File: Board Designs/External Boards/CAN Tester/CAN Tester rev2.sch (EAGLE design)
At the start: 30 parts, among them M1 Minifit-1, M2 Nanofit-1, M3 Nanofit-2, M4 Minifit-2, U1 ISOLATED CAN TRANSCIEVER, U3 TEENSY_3.2_SIMPLE, U4 CHARACTER_LCD

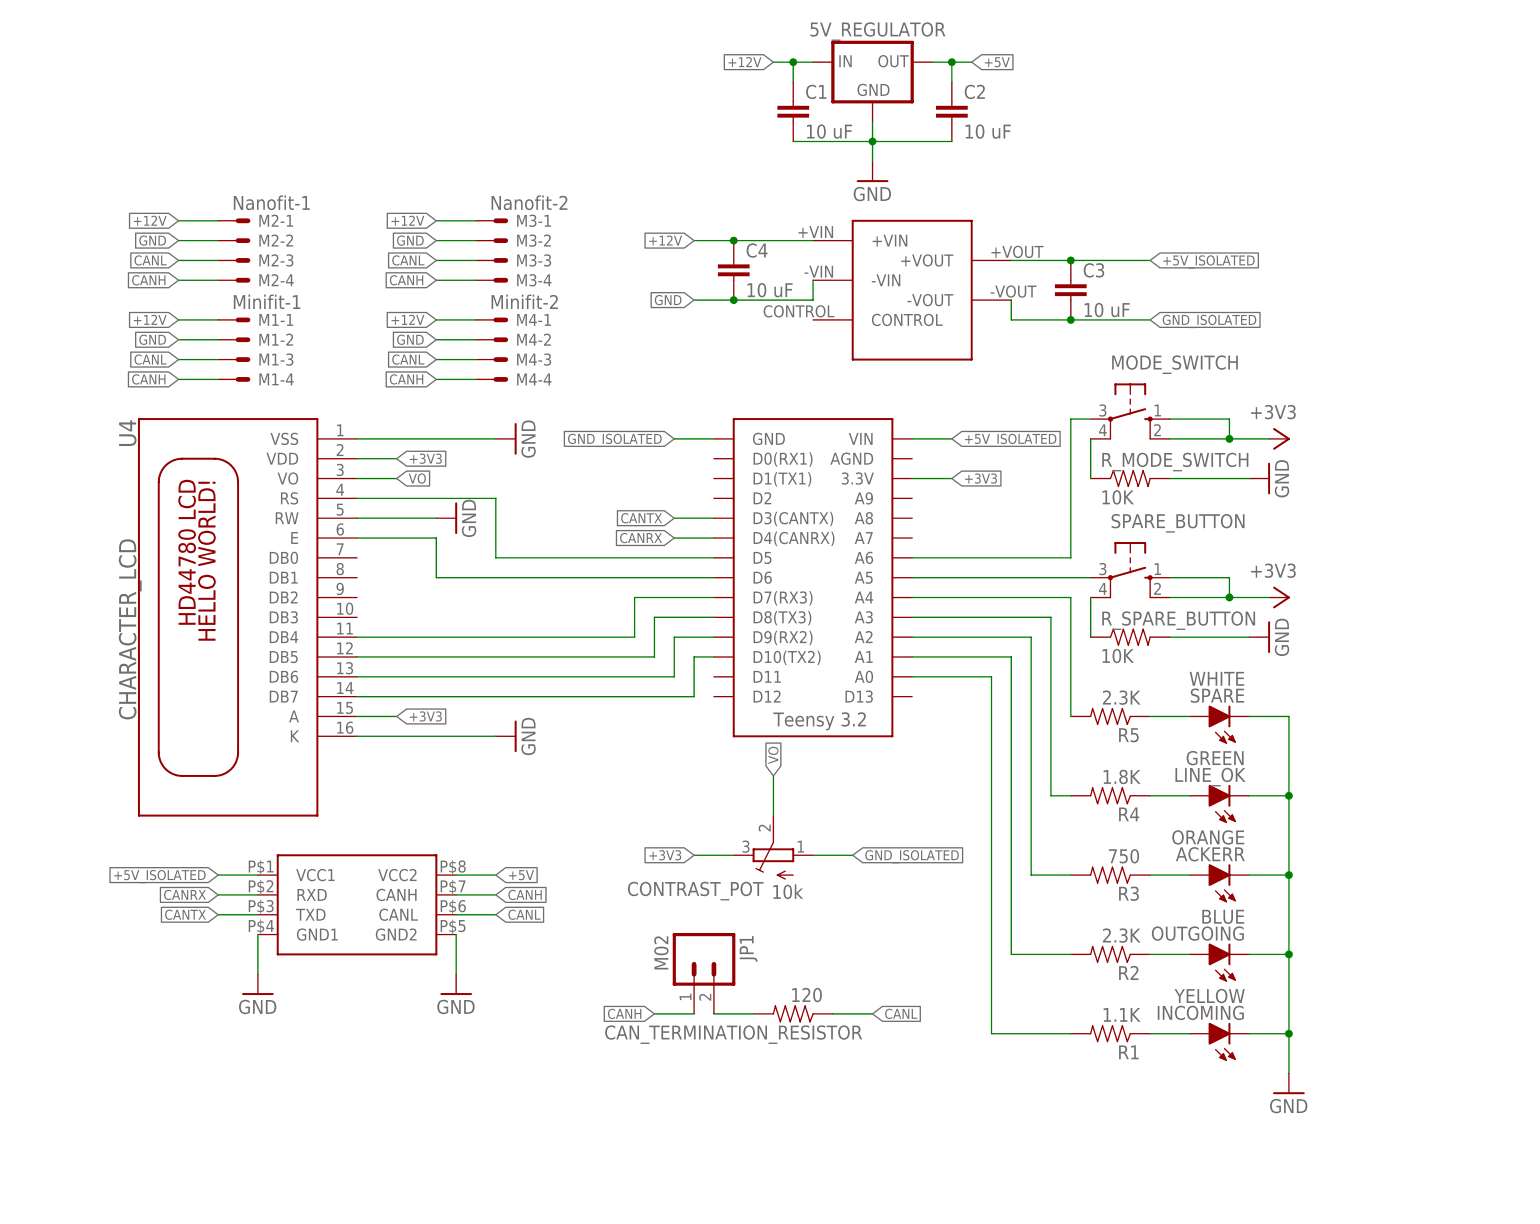
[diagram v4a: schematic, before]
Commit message: Adjusted schematic to make the connections clearer for CAN_Tester, and verified it
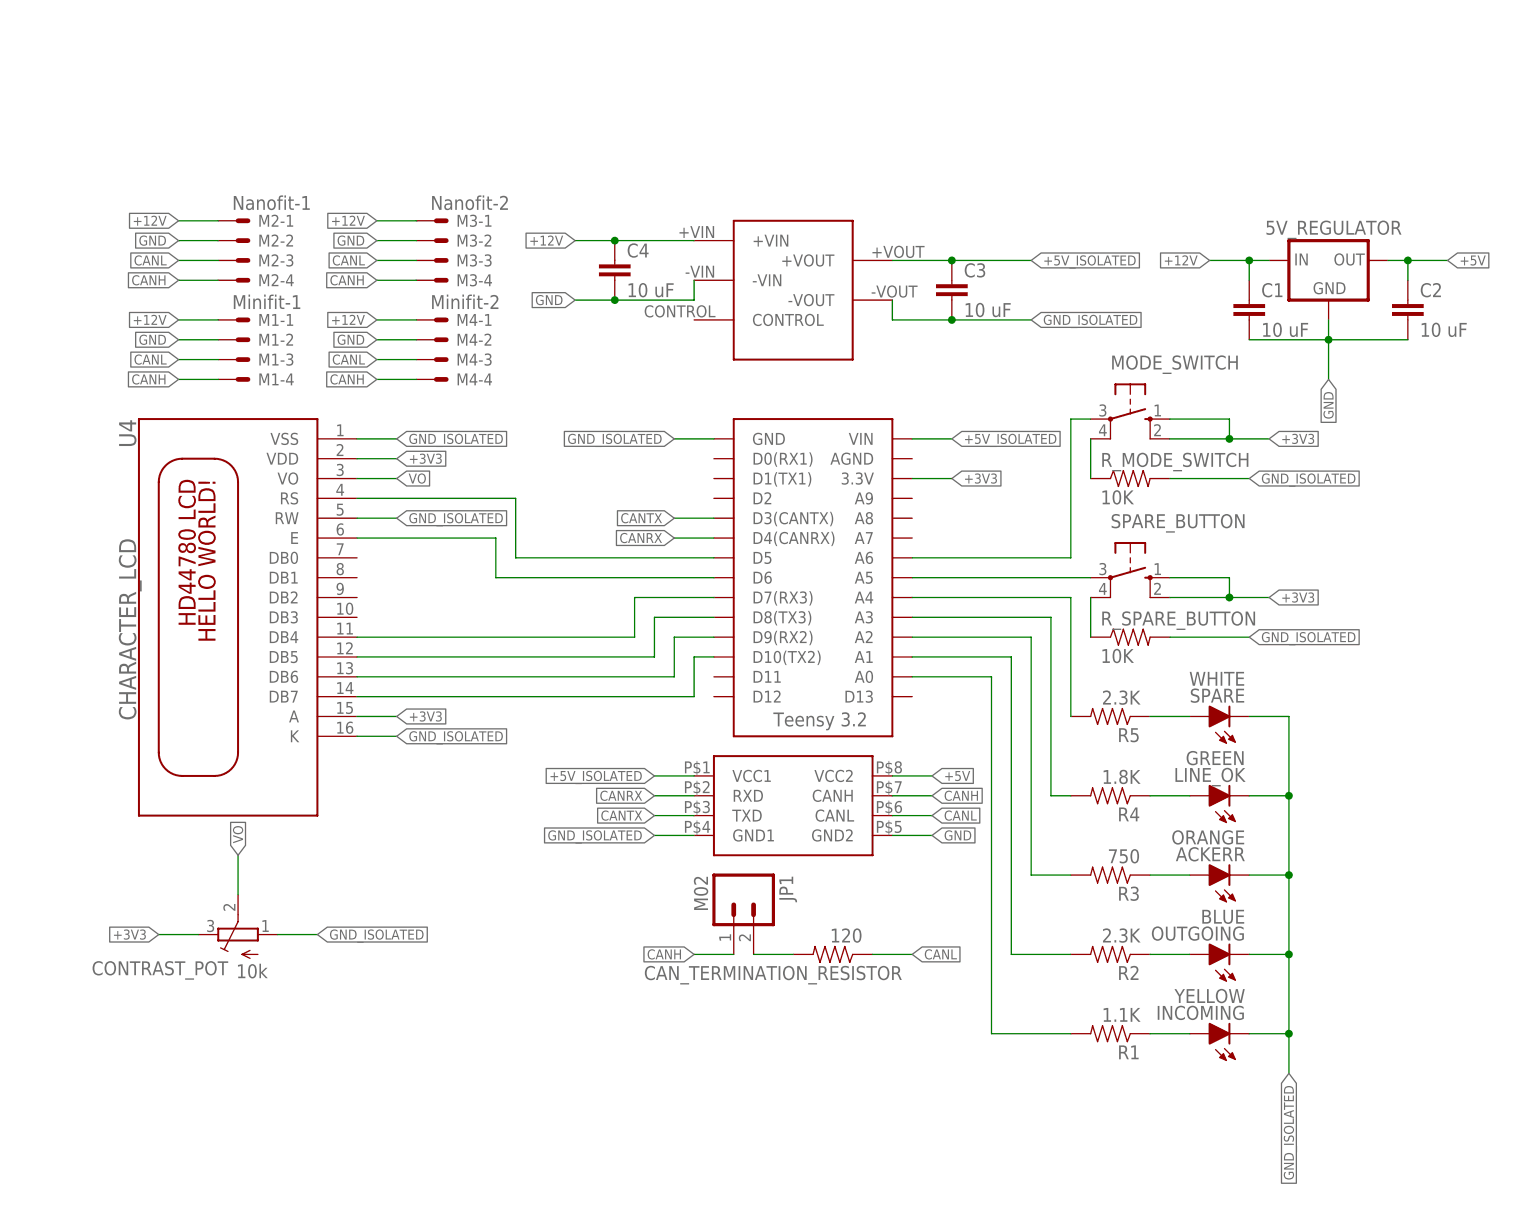
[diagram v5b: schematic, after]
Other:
- moved on the sheet: 5V_REGULATOR, C1, C2, C3, C4, CAN_TERMINATION_RESISTOR, CONTRAST_POT, JP1, M3-1, M3-2, M3-3, M3-4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

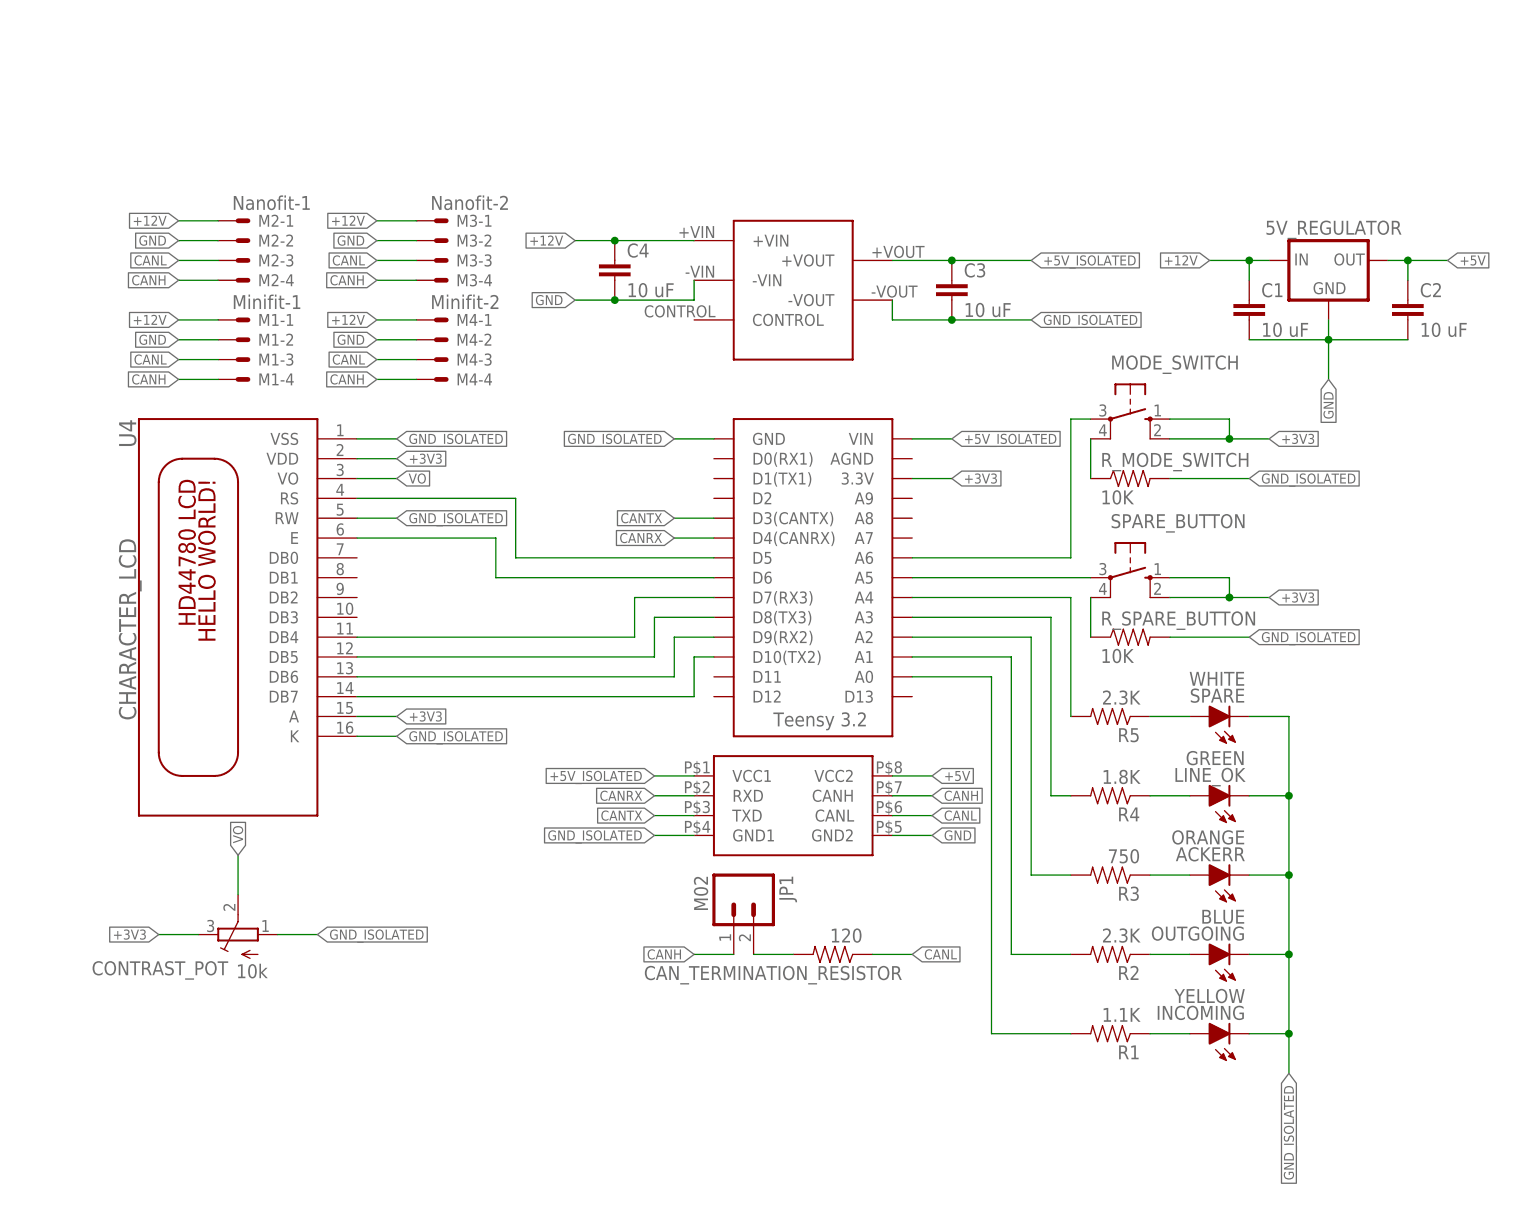
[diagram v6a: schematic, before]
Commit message: Added silkscreen for CAN_Tester Board
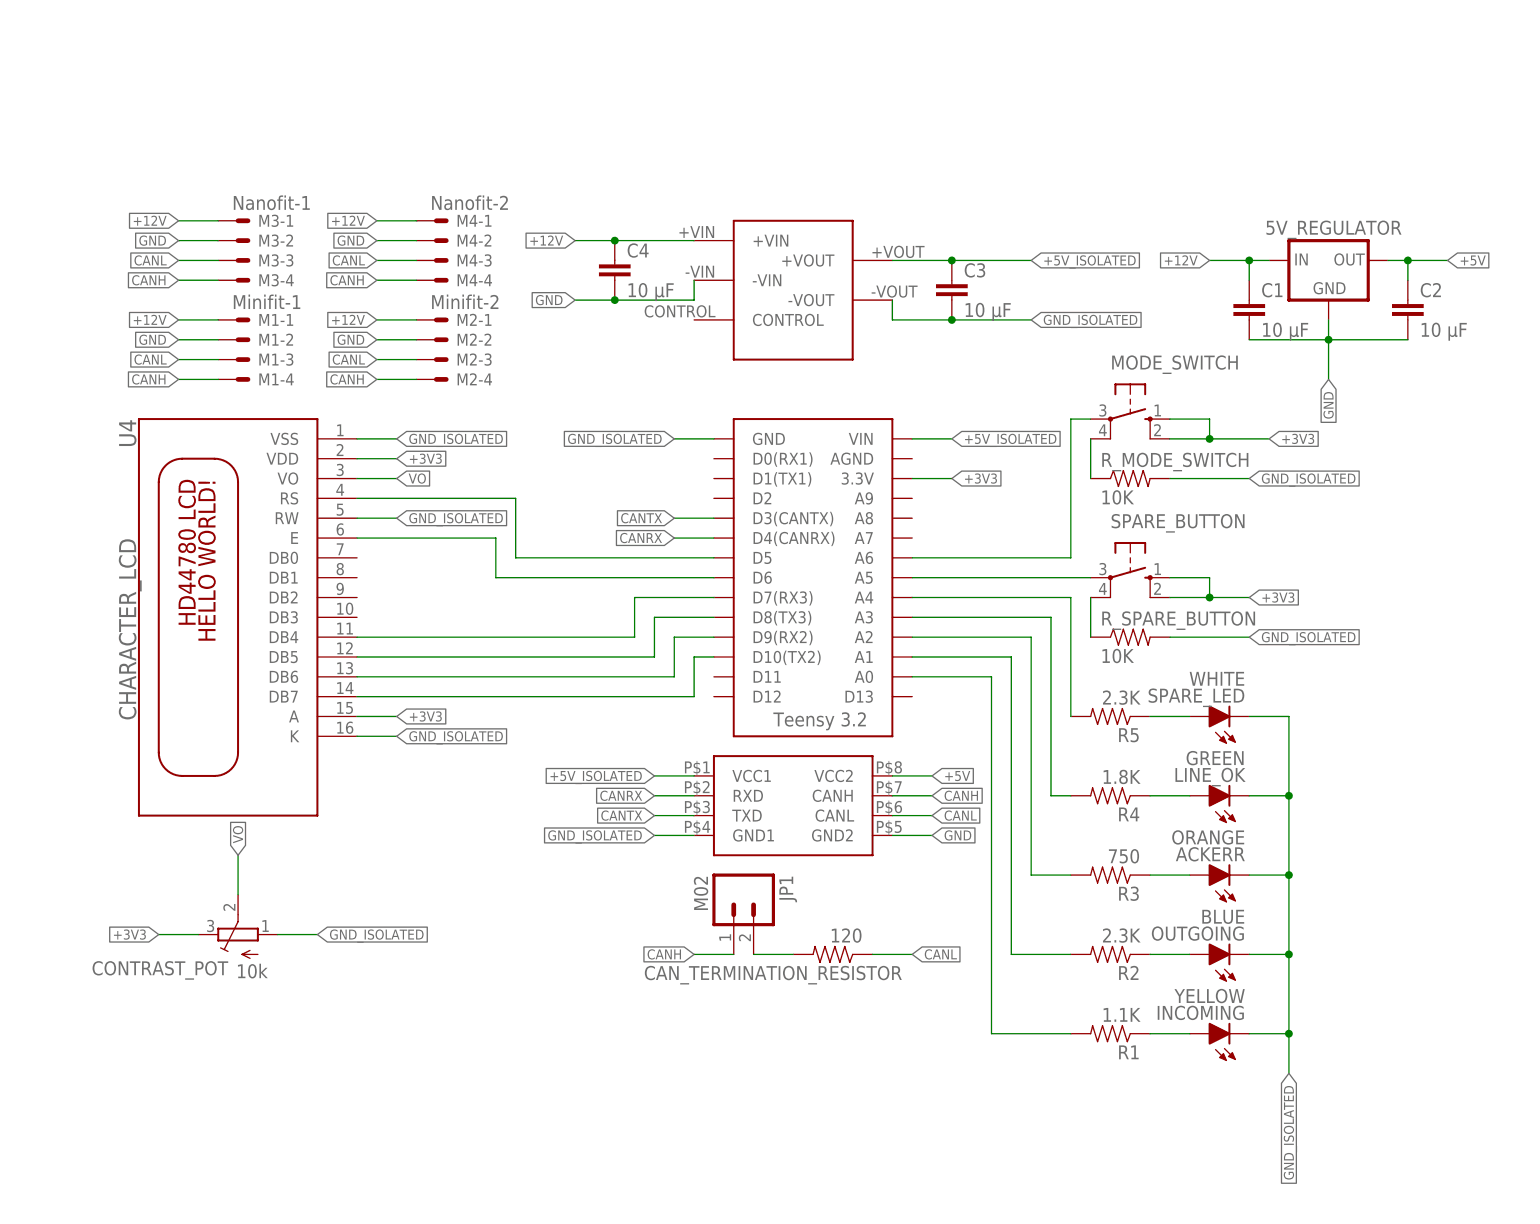
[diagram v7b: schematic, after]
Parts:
- C1, C2, C3, C4: value 10 uF -> 10 μF
- M2: value Nanofit-1 -> Minifit-2; device HyTechDevices:CONNECTOR-4NANO-FIT-VERTICAL-4 -> HyTechDevices:CONNECTOR-4
- M3: value Nanofit-2 -> Nanofit-1
- M4: value Minifit-2 -> Nanofit-2; device HyTechDevices:CONNECTOR-4 -> HyTechDevices:CONNECTOR-4NANO-FIT-VERTICAL-4
- U1: value ISOLATED CAN TRANSCIEVER -> ISOCAN
- renumbered SPARE to SPARE_LED
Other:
- moved on the sheet: M2-1, M2-2, M2-3, M2-4, M3-1, M3-2, M3-3, M3-4, M4-1, M4-2, M4-3, M4-4
